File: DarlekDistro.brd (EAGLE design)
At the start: 100 x 50 mm, 36 parts, among them J1 POWERPOLE_POWER10AWG, J10 FUSEATC, J11 POWERPOLE_POWER10AWG, J12 FUSEATC, J2 FUSEATC, J3 POWERPOLE_POWER10AWG, J4 FUSEATC, J5 POWERPOLE_POWER10AWG, J6 FUSEATC, J7 POWERPOLE_POWER10AWG, J8 FUSEATC, J9 POWERPOLE_POWER10AWG

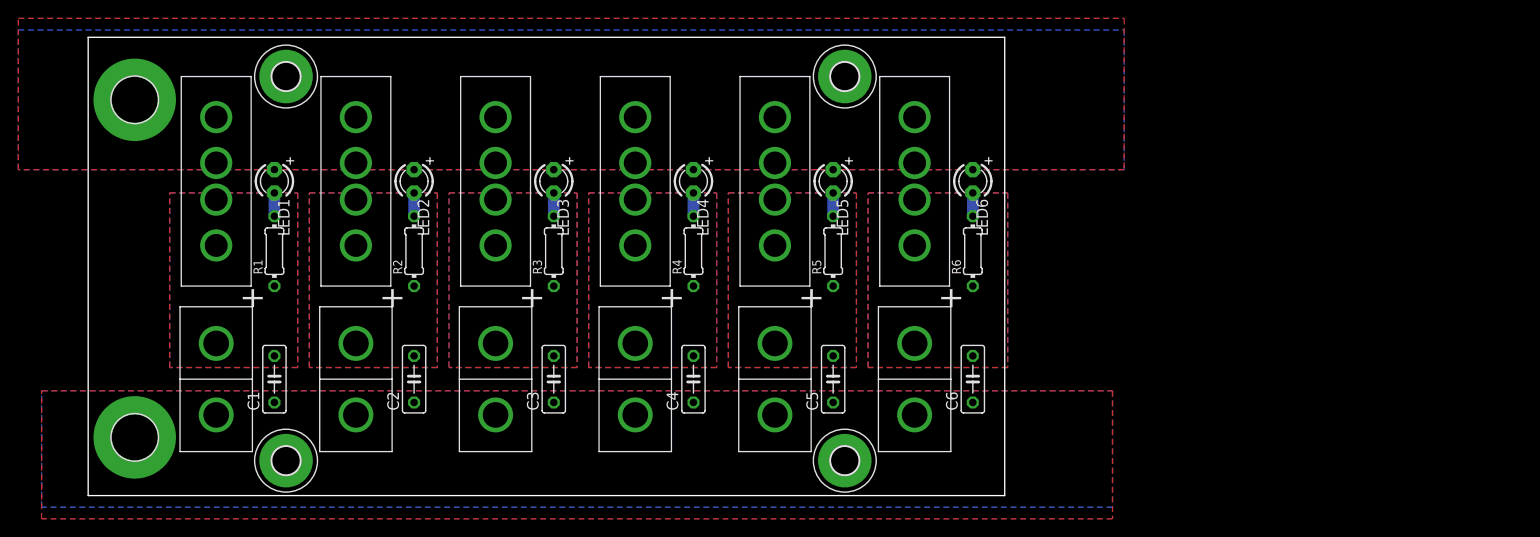
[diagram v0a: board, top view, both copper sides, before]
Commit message: Added 5v reg and connectors
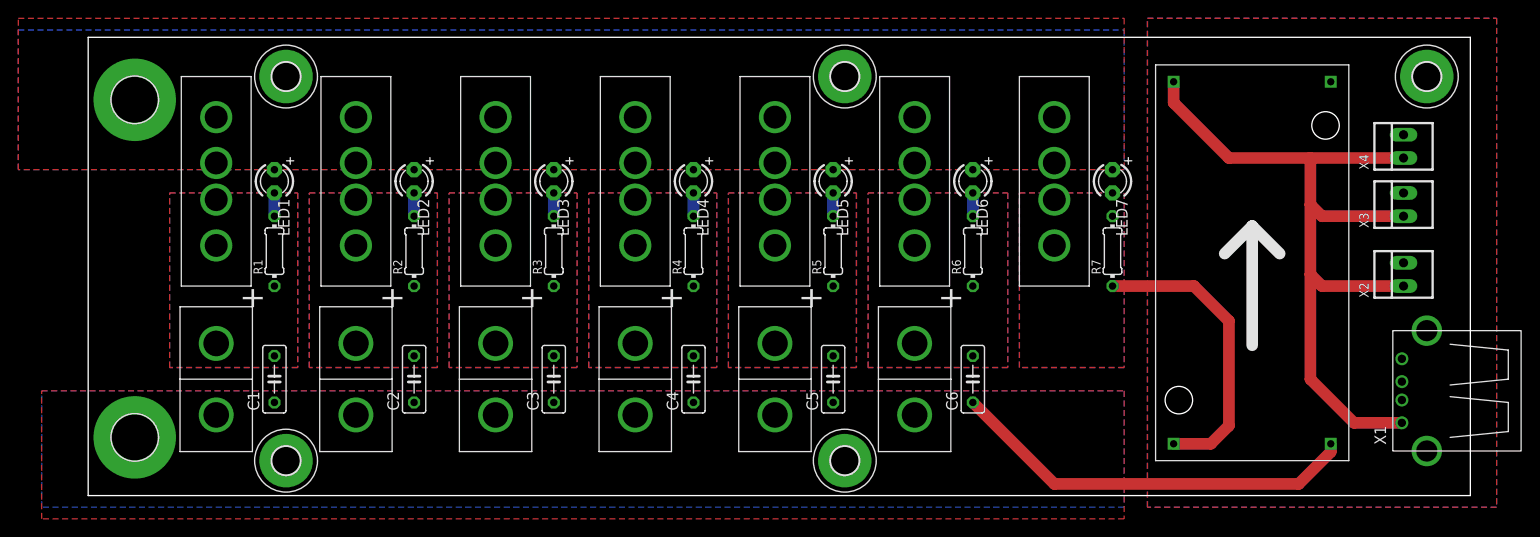
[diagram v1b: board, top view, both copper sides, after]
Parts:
- added H7: MOUNT-PAD-ROUND3.0, holes:3,0-PAD
- added J13: FUSEATC, powerpoles:FUSE_ATC
- added LED7: (no value), adafruit:LED3MM
- added R7: (no value), rcl:0204/7
- added U$1: DSN2596_REG, DarlekParts:DSN2596_REG
- added X1: (no value), con-usb-3:USB-A-H
- added X2, X3, X4: 22-23-2021, con-molex:22-23-2021
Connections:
- new net 5VGND: U$1.P$3, X1.GND, X2.2, X3.2, X4.2
- new net N$7: LED7.K, R7.2
- new net N$8: U$1.P$4, X1.VBUS, X2.1, X3.1, X4.1
- new net PPV7: J13.P$1, J13.P$2, R7.1, U$1.P$1
- net GND: now also U$1.P$2
- net VCC: now also J13.P$3, J13.P$4, LED7.A
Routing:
- net N$8: track 0.00 -> 87.3 mm
- net GND: track 0.00 -> 45.1 mm
- net PPV7: track 0.00 -> 32.6 mm
- added copper zone on layer 1, net 5VGND
- added copper zone on layer 16, net 5VGND
- added copper zone on layer 1, net PPV7
- added copper zone on layer 16, net PPV7
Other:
- board size 100 x 50 mm -> 150.8 x 50 mm
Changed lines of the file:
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@@
 <layer number="220" name="220bmp" color="21" fill="1" visible="no" active="no"/>
 <layer number="221" name="221bmp" color="22" fill="1" visible="no" active="no"/>
+<layer number="222" name="222bmp" color="23" fill="1" visible="no" active="no"/>
 <layer number="223" name="223bmp" color="24" fill="1" visible="no" active="no"/>
 <layer number="224" name="224bmp" color="25" fill="1" visible="no" active="no"/>
@@
 <board>
 <plain>
-<wire x1="0" y1="0" x2="100" y2="0" width="0" layer="20"/>
-<wire x1="100" y1="0" x2="100" y2="50" width="0" layer="20"/>
-<wire x1="100" y1="50" x2="0" y2="50" width="0" layer="20"/>
+<wire x1="0" y1="0" x2="150.8" y2="0" width="0" layer="20"/>
+<wire x1="150.8" y1="0" x2="150.8" y2="50" width="0" layer="20"/>
+<wire x1="150.8" y1="50" x2="0" y2="50" width="0" layer="20"/>
 <wire x1="0" y1="50" x2="0" y2="0" width="0" layer="20"/>
 </plain>
@@
 <element name="H5" library="holes" package="3,0-PAD" value="MOUNT-PAD-ROUND3.0" x="82.55" y="45.72"/>
 <element name="H6" library="holes" package="3,0-PAD" value="MOUNT-PAD-ROUND3.0" x="21.59" y="45.72"/>
+<element name="R7" library="rcl" package="0204/7" value="" x="111.76" y="26.67" rot="R90"/>
+<element name="J13" library="powerpoles" package="FUSE_ATC" value="FUSEATC" x="105.41" y="34.29" rot="R90"/>
+<element name="LED7" library="adafruit" package="LED3MM" value="" x="111.76" y="34.29" rot="R270"/>
+<element name="U$1" library="DarlekParts" package="DSN2596_REG" value="DSN2596_REG" x="127" y="25.4" rot="R90"/>
+<element name="X1" library="con-usb-3" package="USB-A-H" value="" x="146.05" y="11.43" rot="R180"/>
+<element name="X2" library="con-molex" package="22-23-2021" value="22-23-2021" x="143.51" y="24.13" rot="R90">
+<attribute name="OC_NEWARK" value="25C3832" x="143.51" y="24.13" size="1.778" layer="27" rot="R90" display="off"/>
+<attribute name="MPN" value="22-23-2021" x="143.51" y="24.13" size="1.778" layer="27" rot="R90" display="off"/>
+<attribute name="MF" value="MOLEX" x="143.51" y="24.13" size="1.778" layer="27" rot="R90" display="off"/>
+<attribute name="OC_FARNELL" value="1462926" x="143.51" y="24.13" size="1.778" layer="27" rot="R90" display="off"/>
+</element>
+<element name="X3" library="con-molex" package="22-23-2021" value="22-23-2021" x="143.51" y="31.75" rot="R90">
+<attribute name="OC_NEWARK" value="25C3832" x="143.51" y="31.75" size="1.778" layer="27" rot="R90" display="off"/>
+<attribute name="MPN" value="22-23-2021" x="143.51" y="31.75" size="1.778" layer="27" rot="R90" display="off"/>
+<attribute name="MF" value="MOLEX" x="143.51" y="31.75" size="1.778" layer="27" rot="R90" display="off"/>
+<attribute name="OC_FARNELL" value="1462926" x="143.51" y="31.75" size="1.778" layer="27" rot="R90" display="off"/>
+</element>
+<element name="X4" library="con-molex" package="22-23-2021" value="22-23-2021" x="143.51" y="38.1" rot="R90">
+<attribute name="OC_NEWARK" value="25C3832" x="143.51" y="38.1" size="1.778" layer="27" rot="R90" display="off"/>
+<attribute name="MPN" value="22-23-2021" x="143.51" y="38.1" size="1.778" layer="27" rot="R90" display="off"/>
+<attribute name="MF" value="MOLEX" x="143.51" y="38.1" size="1.778" layer="27" rot="R90" display="off"/>
+<attribute name="OC_FARNELL" value="1462926" x="143.51" y="38.1" size="1.778" layer="27" rot="R90" display="off"/>
+</element>
+<element name="H7" library="holes" package="3,0-PAD" value="MOUNT-PAD-ROUND3.0" x="146.05" y="45.72"/>
 </elements>
 <signals>
@@
 <polygon width="0.4064" layer="16" thermals="no">
 <vertex x="-5.08" y="11.43"/>
-<vertex x="111.76" y="11.43"/>
-<vertex x="111.76" y="-1.27"/>
+<vertex x="113.03" y="11.43"/>
+<vertex x="113.03" y="-1.27"/>
 <vertex x="-5.08" y="-1.27"/>
 </polygon>
@@
 <polygon width="0.4064" layer="1" thermals="no">
 <vertex x="-5.08" y="11.43"/>
-<vertex x="111.76" y="11.43"/>
-<vertex x="111.76" y="-2.54"/>
+<vertex x="113.03" y="11.43"/>
+<vertex x="113.03" y="-2.54"/>
 <vertex x="-5.08" y="-2.54"/>
 </polygon>
+<contactref element="U$1" pad="P$2"/>
+<wire x1="135.5725" y1="5.6515" x2="135.5725" y2="4.7625" width="1.27" layer="1"/>
+<wire x1="135.5725" y1="4.7625" x2="132.08" y2="1.27" width="1.27" layer="1"/>
+<wire x1="132.08" y1="1.27" x2="105.41" y2="1.27" width="1.27" layer="1"/>
+<wire x1="105.41" y1="1.27" x2="96.52" y2="10.16" width="1.27" layer="1"/>
 </signal>
 <signal name="PPV1">
@@
 <vertex x="-7.62" y="35.56"/>
 </polygon>
+<contactref element="LED7" pad="A"/>
+<contactref element="J13" pad="P$4"/>
+<contactref element="J13" pad="P$3"/>
 </signal>
 <signal name="PPV2">
@@
 <wire x1="96.52" y1="30.48" x2="96.52" y2="33.02" width="1.27" layer="16"/>
 </signal>
+<signal name="PPV7">
+<contactref element="J13" pad="P$2"/>
+<contactref element="J13" pad="P$1"/>
+<contactref element="R7" pad="1"/>
+<contactref element="U$1" pad="P$1"/>
+<polygon width="0.4064" layer="16" thermals="no">
+<vertex x="101.6" y="33.02"/>
+<vertex x="113.03" y="33.02"/>
+<vertex x="113.03" y="13.97"/>
+<vertex x="101.6" y="13.97"/>
+</polygon>
+<polygon width="0.4064" layer="1" thermals="no">
+<vertex x="101.6" y="33.02"/>
+<vertex x="113.03" y="33.02"/>
+<vertex x="113.03" y="13.97"/>
+<vertex x="101.6" y="13.97"/>
+</polygon>
+<wire x1="118.4275" y1="5.6515" x2="122.4915" y2="5.6515" width="1.27" layer="1"/>
+<wire x1="122.4915" y1="5.6515" x2="124.46" y2="7.62" width="1.27" layer="1"/>
+<wire x1="124.46" y1="7.62" x2="124.46" y2="19.05" width="1.27" layer="1"/>
+<wire x1="124.46" y1="19.05" x2="120.65" y2="22.86" width="1.27" layer="1"/>
+<wire x1="120.65" y1="22.86" x2="111.76" y2="22.86" width="1.27" layer="1"/>
+</signal>
+<signal name="N$7">
+<contactref element="R7" pad="2"/>
+<contactref element="LED7" pad="K"/>
+<wire x1="111.76" y1="30.48" x2="111.76" y2="33.02" width="0" layer="19" extent="1-1"/>
+</signal>
+<signal name="N$8">
+<contactref element="U$1" pad="P$4"/>
+<contactref element="X1" pad="VBUS"/>
+<contactref element="X4" pad="1"/>
+<contactref element="X3" pad="1"/>
+<contactref element="X2" pad="1"/>
+<wire x1="118.4275" y1="45.1485" x2="118.4275" y2="42.8625" width="1.27" layer="1"/>
+<wire x1="118.4275" y1="42.8625" x2="124.46" y2="36.83" width="1.27" layer="1"/>
+<wire x1="124.46" y1="36.83" x2="133.35" y2="36.83" width="1.27" layer="1"/>
+<wire x1="133.35" y1="36.83" x2="143.51" y2="36.83" width="1.27" layer="1"/>
+<wire x1="143.51" y1="30.48" x2="134.62" y2="30.48" width="1.27" layer="1"/>
+<wire x1="134.62" y1="30.48" x2="133.35" y2="31.75" width="1.27" layer="1"/>
+<wire x1="133.35" y1="31.75" x2="133.35" y2="36.83" width="1.27" layer="1"/>
+<wire x1="143.51" y1="22.86" x2="134.62" y2="22.86" width="1.27" layer="1"/>
+<wire x1="134.62" y1="22.86" x2="133.35" y2="24.13" width="1.27" layer="1"/>
+<wire x1="133.35" y1="24.13" x2="133.35" y2="31.75" width="1.27" layer="1"/>
+<wire x1="143.3322" y1="7.9375" x2="138.1125" y2="7.9375" width="1.27" layer="1"/>
+<wire x1="138.1125" y1="7.9375" x2="133.35" y2="12.7" width="1.27" layer="1"/>
+<wire x1="133.35" y1="12.7" x2="133.35" y2="24.13" width="1.27" layer="1"/>
+</signal>
+<signal name="5VGND">
+<contactref element="U$1" pad="P$3"/>
+<contactref element="X1" pad="GND"/>
+<contactref element="X4" pad="2"/>
+<contactref element="X3" pad="2"/>
+<contactref element="X2" pad="2"/>
+<polygon width="0.4064" layer="16" thermals="no">
+<vertex x="115.57" y="52.07"/>
+<vertex x="153.67" y="52.07"/>
+<vertex x="153.67" y="-1.27"/>
+<vertex x="115.57" y="-1.27"/>
+</polygon>
+<polygon width="0.4064" layer="1" thermals="no">
+<vertex x="115.57" y="52.07"/>
+<vertex x="153.67" y="52.07"/>
+<vertex x="153.67" y="-1.27"/>
+<vertex x="115.57" y="-1.27"/>
+</polygon>
+</signal>
 </signals>
